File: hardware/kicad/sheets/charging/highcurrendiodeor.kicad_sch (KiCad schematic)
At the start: 8 parts, among them CN6 5017, Q3 CSD17577Q5A, U24 LM5050MKX-1/NOPB

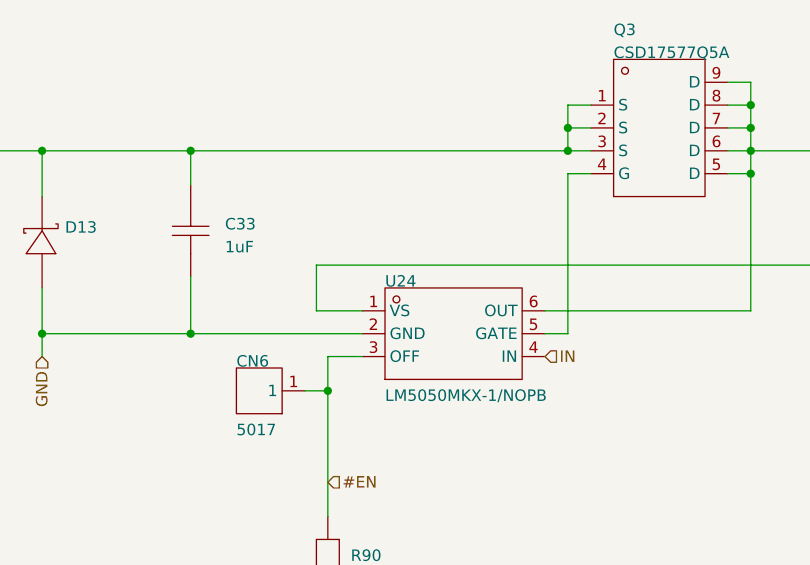
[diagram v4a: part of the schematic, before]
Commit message: 5v usb c done, esc mostly done
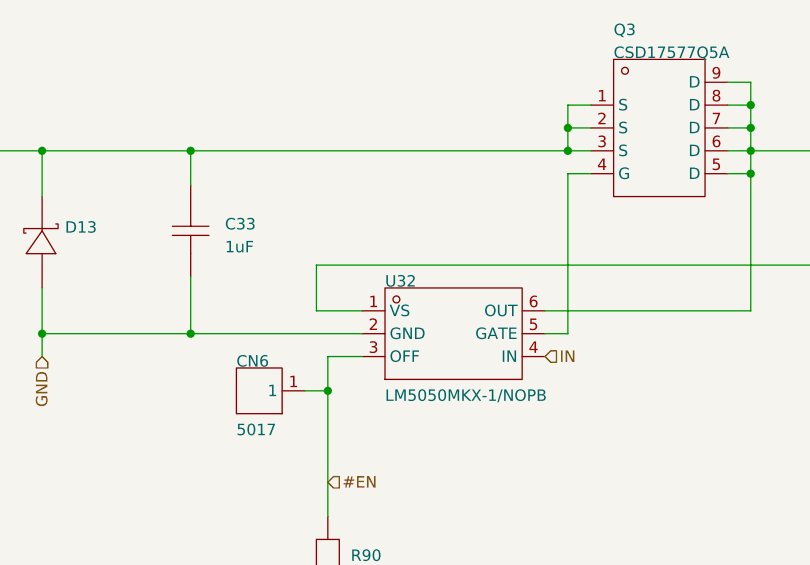
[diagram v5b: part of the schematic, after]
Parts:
- renumbered U24 to U32
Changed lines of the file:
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@@
 			(project "svea_powerboard_rev3"
 				(path "/3f85abf4-0b95-4c4a-b7e9-06f59ca1ea3d/5c2e021f-c2d4-49e2-8c36-9a64f1f12001/8eee6623-4878-45b2-bdab-0e37d3220c38"
-					(reference "R116")
+					(reference "R115")
 					(unit 1)
 				)
@@
 				)
 				(path "/3f85abf4-0b95-4c4a-b7e9-06f59ca1ea3d/5c2e021f-c2d4-49e2-8c36-9a64f1f12001/d932e0fc-7b09-4e74-a033-a342c08a0a15"
-					(reference "R126")
+					(reference "R124")
 					(unit 1)
 				)
 				(path "/3f85abf4-0b95-4c4a-b7e9-06f59ca1ea3d/5c2e021f-c2d4-49e2-8c36-9a64f1f12001/dbcfb661-1d23-45dc-813f-0febc1515a98"
-					(reference "R114")
+					(reference "R113")
 					(unit 1)
 				)
@@
 			(project "svea_powerboard_rev3"
 				(path "/3f85abf4-0b95-4c4a-b7e9-06f59ca1ea3d/5c2e021f-c2d4-49e2-8c36-9a64f1f12001/8eee6623-4878-45b2-bdab-0e37d3220c38"
-					(reference "R117")
+					(reference "R116")
 					(unit 1)
 				)
@@
 				)
 				(path "/3f85abf4-0b95-4c4a-b7e9-06f59ca1ea3d/5c2e021f-c2d4-49e2-8c36-9a64f1f12001/d932e0fc-7b09-4e74-a033-a342c08a0a15"
-					(reference "R127")
+					(reference "R125")
 					(unit 1)
 				)
 				(path "/3f85abf4-0b95-4c4a-b7e9-06f59ca1ea3d/5c2e021f-c2d4-49e2-8c36-9a64f1f12001/dbcfb661-1d23-45dc-813f-0febc1515a98"
-					(reference "R115")
+					(reference "R114")
 					(unit 1)
 				)
@@
 		(on_board yes)
 		(dnp no)
-		(property "Reference" "#PWR082"
+		(property "Reference" "#PWR083"
 			(at 151.13 129.54 0)
 			(effects
@@
 			(project "svea_powerboard_rev3"
 				(path "/3f85abf4-0b95-4c4a-b7e9-06f59ca1ea3d/5c2e021f-c2d4-49e2-8c36-9a64f1f12001/8eee6623-4878-45b2-bdab-0e37d3220c38"
-					(reference "#PWR0105")
+					(reference "#PWR0103")
 					(unit 1)
 				)
 				(path "/3f85abf4-0b95-4c4a-b7e9-06f59ca1ea3d/5c2e021f-c2d4-49e2-8c36-9a64f1f12001/a048a8c1-de8c-4417-9e40-d40a18f390ce"
-					(reference "#PWR082")
+					(reference "#PWR083")
 					(unit 1)
 				)
 				(path "/3f85abf4-0b95-4c4a-b7e9-06f59ca1ea3d/5c2e021f-c2d4-49e2-8c36-9a64f1f12001/ad660ab0-1da6-44b7-9096-9ee4c3bc2383"
-					(reference "#PWR083")
+					(reference "#PWR084")
 					(unit 1)
 				)
 				(path "/3f85abf4-0b95-4c4a-b7e9-06f59ca1ea3d/5c2e021f-c2d4-49e2-8c36-9a64f1f12001/ca919776-c91b-4883-8f90-f75d19396b00"
-					(reference "#PWR084")
+					(reference "#PWR085")
 					(unit 1)
 				)
 				(path "/3f85abf4-0b95-4c4a-b7e9-06f59ca1ea3d/5c2e021f-c2d4-49e2-8c36-9a64f1f12001/d932e0fc-7b09-4e74-a033-a342c08a0a15"
-					(reference "#PWR0114")
+					(reference "#PWR0112")
 					(unit 1)
 				)
 				(path "/3f85abf4-0b95-4c4a-b7e9-06f59ca1ea3d/5c2e021f-c2d4-49e2-8c36-9a64f1f12001/dbcfb661-1d23-45dc-813f-0febc1515a98"
-					(reference "#PWR0104")
+					(reference "#PWR0102")
 					(unit 1)
 				)
@@
 		(on_board yes)
 		(dnp no)
-		(property "Reference" "U24"
+		(property "Reference" "U32"
 			(at 157.48 92.71 0)
 			(effects
@@
 			(project "svea_powerboard_rev3"
 				(path "/3f85abf4-0b95-4c4a-b7e9-06f59ca1ea3d/5c2e021f-c2d4-49e2-8c36-9a64f1f12001/8eee6623-4878-45b2-bdab-0e37d3220c38"
-					(reference "U36")
+					(reference "U44")
 					(unit 1)
 				)
 				(path "/3f85abf4-0b95-4c4a-b7e9-06f59ca1ea3d/5c2e021f-c2d4-49e2-8c36-9a64f1f12001/a048a8c1-de8c-4417-9e40-d40a18f390ce"
-					(reference "U24")
+					(reference "U32")
 					(unit 1)
 				)
 				(path "/3f85abf4-0b95-4c4a-b7e9-06f59ca1ea3d/5c2e021f-c2d4-49e2-8c36-9a64f1f12001/ad660ab0-1da6-44b7-9096-9ee4c3bc2383"
-					(reference "U25")
+					(reference "U33")
 					(unit 1)
 				)
 				(path "/3f85abf4-0b95-4c4a-b7e9-06f59ca1ea3d/5c2e021f-c2d4-49e2-8c36-9a64f1f12001/ca919776-c91b-4883-8f90-f75d19396b00"
-					(reference "U26")
+					(reference "U34")
 					(unit 1)
 				)
 				(path "/3f85abf4-0b95-4c4a-b7e9-06f59ca1ea3d/5c2e021f-c2d4-49e2-8c36-9a64f1f12001/d932e0fc-7b09-4e74-a033-a342c08a0a15"
-					(reference "U39")
+					(reference "U47")
 					(unit 1)
 				)
 				(path "/3f85abf4-0b95-4c4a-b7e9-06f59ca1ea3d/5c2e021f-c2d4-49e2-8c36-9a64f1f12001/dbcfb661-1d23-45dc-813f-0febc1515a98"
-					(reference "U35")
-					(unit 1)
-				)
+					(reference "U43")
+					(unit 1)
+				)

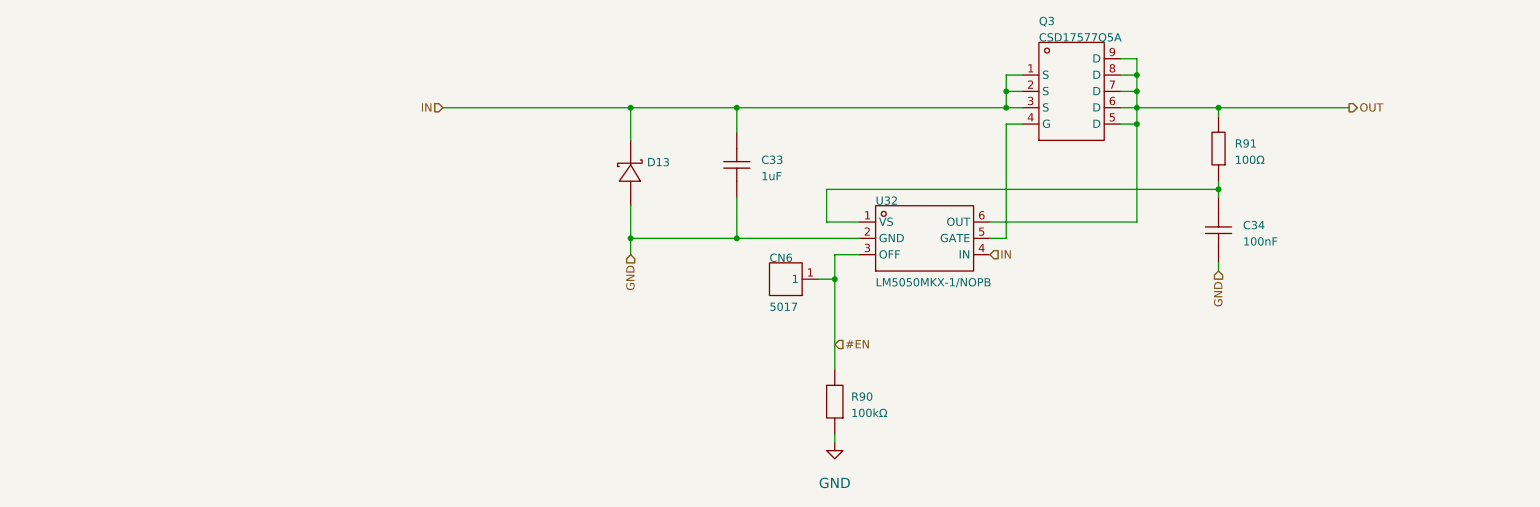
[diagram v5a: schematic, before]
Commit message: ideal diode initial layout and some fixes
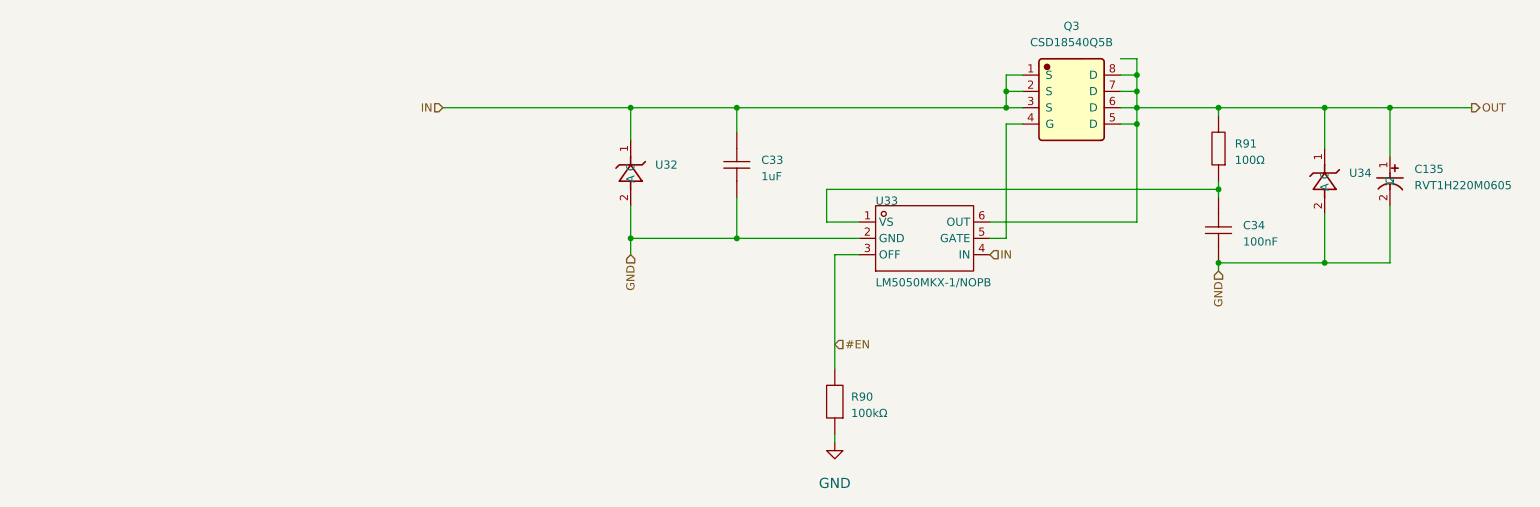
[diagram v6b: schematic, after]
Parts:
- removed CN6: 5017, 5v rail sm-easyedapro:CONN-SMD_5017, symbol 5v rail sm-easyedapro:5017_C9900015874
- removed D13: ~, 5v rail sm-easyedapro:SMA_L4.4-W2.8-LS5.4-RD, symbol 5v rail sm-easyedapro:SS16T3G
- removed Q3: CSD17577Q5A, 5v rail sm-easyedapro:DFN-8_L5.8-W4.9-P1.27-LS6.0-BL-1, symbol 5v rail sm-easyedapro:CSD17577Q5A
- added C135: RVT1H220M0605, JLCImport:RVT1H220M0605, symbol JLCImport:RVT1H220M0605
- added Q3: CSD18540Q5B, JLCImport:CSD18540Q5B, symbol JLCImport:CSD18540Q5B
- added U32, U34: SMBJ24A_C19077578, JLCImport:SMBJ24A_C19077578, symbol JLCImport:SMBJ24A_C19077578
- renumbered U32 to U33
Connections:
- net GND: now also C135.2, U32.2 (A), U34.2 (A)
- net IN: now also Q3.1 (S), Q3.2 (S), Q3.3 (S), U32.1 (C)
- net OUT: now also C135.1, Q3.5 (D), Q3.6 (D), Q3.7 (D), Q3.8 (D), U34.1 (C)
- net at U33.5 (GATE): now also Q3.4 (G)

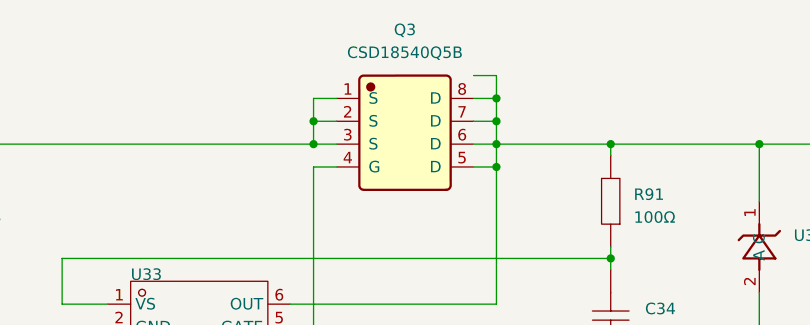
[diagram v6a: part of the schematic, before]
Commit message: various changes, update ideal diode to a more approp fet
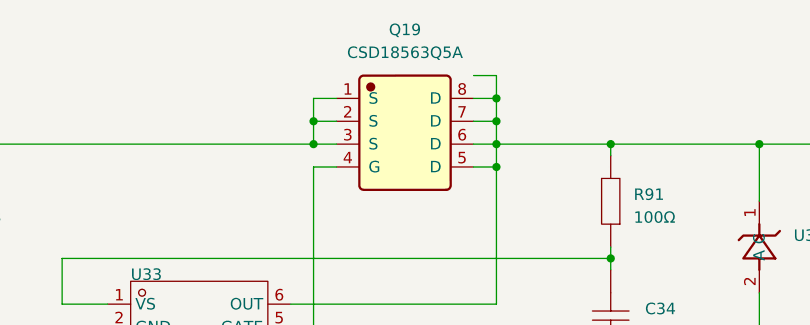
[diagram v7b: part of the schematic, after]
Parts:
- removed Q3: CSD18540Q5B, JLCImport:CSD18540Q5B, symbol JLCImport:CSD18540Q5B
- added Q19: CSD18563Q5A, JLCImport:CSD18563Q5A, symbol JLCImport:CSD18563Q5A
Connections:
- net IN: now also Q19.1 (S), Q19.2 (S), Q19.3 (S)
- net OUT: now also Q19.5 (D), Q19.6 (D), Q19.7 (D), Q19.8 (D)
- net at U33.5 (GATE): now also Q19.4 (G)
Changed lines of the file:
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@@
 	)
 	(symbol
-		(lib_id "JLCImport:CSD18540Q5B")
+		(lib_id "JLCImport:CSD18563Q5A")
 		(at 187.96 76.2 0)
 		(unit 1)
@@
 		(dnp no)
 		(fields_autoplaced yes)
-		(property "Reference" "Q3"
+		(property "Reference" "Q19"
 			(at 187.96 64.77 0)
 			(effects
@@
 			)
 		)
-		(property "Value" "CSD18540Q5B"
+		(property "Value" "CSD18563Q5A"
 			(at 187.96 67.31 0)
 			(effects
@@
 			)
 		)
-		(property "Footprint" "JLCImport:CSD18540Q5B"
+		(property "Footprint" "JLCImport:CSD18563Q5A"
 			(at 187.96 76.2 0)
 			(effects
@@
 			)
 		)
-		(property "Datasheet" "https://item.szlcsc.com/202942.html"
+		(property "Datasheet" "https://atta.szlcsc.com/upload/public/pdf/source/20200113/C461954_2B67A8A51D2D89EB09DD73C2429BC8A9.pdf"
 			(at 187.96 76.2 0)
 			(effects
@@
 			)
 		)
-		(property "LCSC" "C86513"
+		(property "LCSC" "C77239"
 			(at 187.96 76.2 0)
 			(effects
@@
 			)
 		)
-		(property "Manufacturer Part" "CSD18540Q5B"
+		(property "Manufacturer Part" "CSD18563Q5A"
 			(at 187.96 76.2 0)
 			(effects
@@
 		(pin "1"
 		)
+		(pin "8"
+		)
 		(pin "7"
+		)
+		(pin "3"
 		)
 		(pin "2"
 		)
-		(pin "8"
+		(pin "4"
 		)
 		(pin "6"
-		)
-		(pin "4"
-		)
-		(pin "3"
 		)
 		(pin "5"
@@
 			(project ""
 				(path "/3f85abf4-0b95-4c4a-b7e9-06f59ca1ea3d/5c2e021f-c2d4-49e2-8c36-9a64f1f12001/8eee6623-4878-45b2-bdab-0e37d3220c38"
-					(reference "Q7")
+					(reference "Q23")
 					(unit 1)
 				)
 				(path "/3f85abf4-0b95-4c4a-b7e9-06f59ca1ea3d/5c2e021f-c2d4-49e2-8c36-9a64f1f12001/a048a8c1-de8c-4417-9e40-d40a18f390ce"
-					(reference "Q3")
+					(reference "Q19")
 					(unit 1)
 				)
 				(path "/3f85abf4-0b95-4c4a-b7e9-06f59ca1ea3d/5c2e021f-c2d4-49e2-8c36-9a64f1f12001/ad660ab0-1da6-44b7-9096-9ee4c3bc2383"
-					(reference "Q4")
+					(reference "Q20")
 					(unit 1)
 				)
 				(path "/3f85abf4-0b95-4c4a-b7e9-06f59ca1ea3d/5c2e021f-c2d4-49e2-8c36-9a64f1f12001/ca919776-c91b-4883-8f90-f75d19396b00"
-					(reference "Q5")
+					(reference "Q21")
 					(unit 1)
 				)
 				(path "/3f85abf4-0b95-4c4a-b7e9-06f59ca1ea3d/5c2e021f-c2d4-49e2-8c36-9a64f1f12001/d932e0fc-7b09-4e74-a033-a342c08a0a15"
-					(reference "Q8")
+					(reference "Q24")
 					(unit 1)
 				)
 				(path "/3f85abf4-0b95-4c4a-b7e9-06f59ca1ea3d/5c2e021f-c2d4-49e2-8c36-9a64f1f12001/dbcfb661-1d23-45dc-813f-0febc1515a98"
-					(reference "Q6")
+					(reference "Q22")
 					(unit 1)
 				)
